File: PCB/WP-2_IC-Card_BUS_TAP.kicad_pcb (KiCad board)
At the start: 2 copper layers, 59.4 x 79.1 mm, 12 parts, among them J1 SMS-138-01-G-S, J2 Conn_02x19_Odd_Even, J3 TMS-138-01

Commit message: bus tap
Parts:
- moved key 1.84 mm to (102.1, 70.1)
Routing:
- net GND: vias 92 -> 93
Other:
- board text added: "GND /DET CE2 /CE1 /OE D0 D1 D2 D3 D4 D5 D6 D7 T2 S1 S2 A17 A16 A15 A14 A13 A12 A11 A10 A9 A8 A7 A6 A5 A4 A3 A2 A1 A0 R/W S3 BCHK VCC"
- board text added: "VCC"
- board text removed: "VBUS"

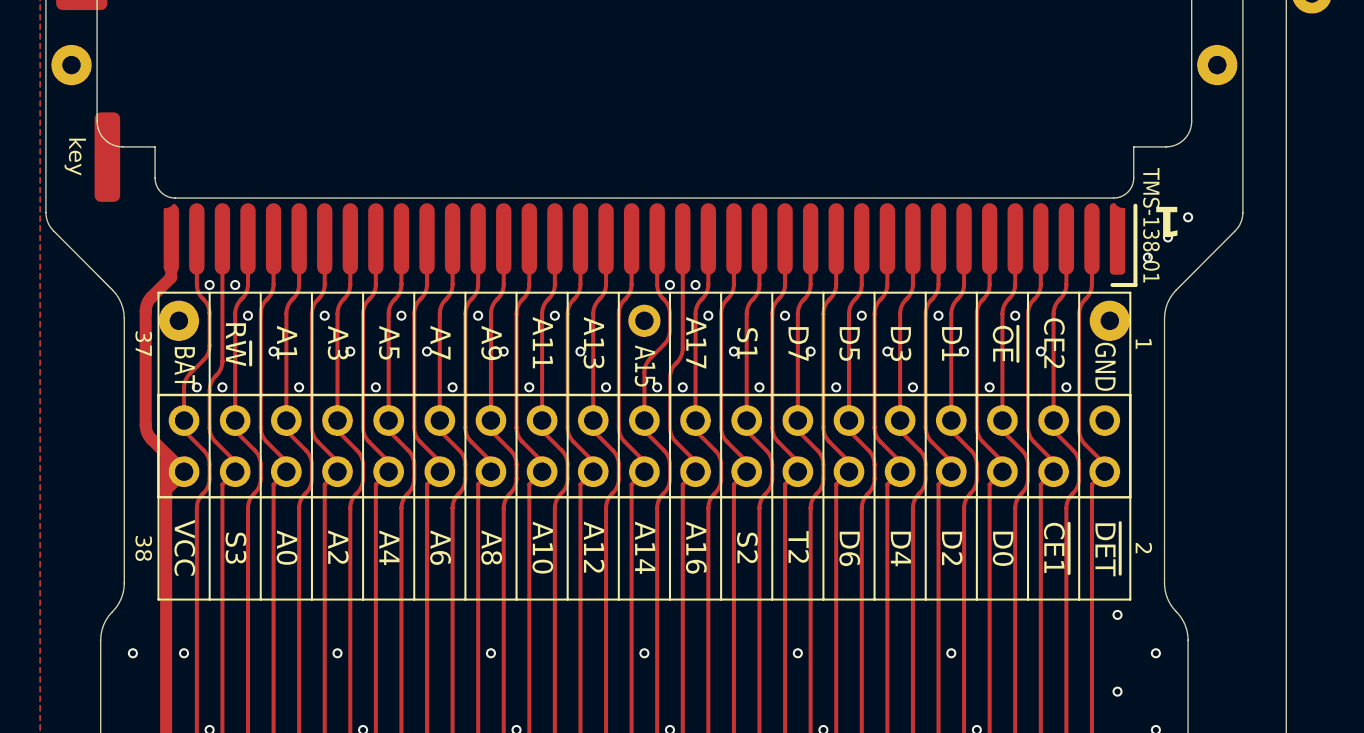
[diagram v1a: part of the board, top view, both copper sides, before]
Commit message: bus tap heal edge cuts
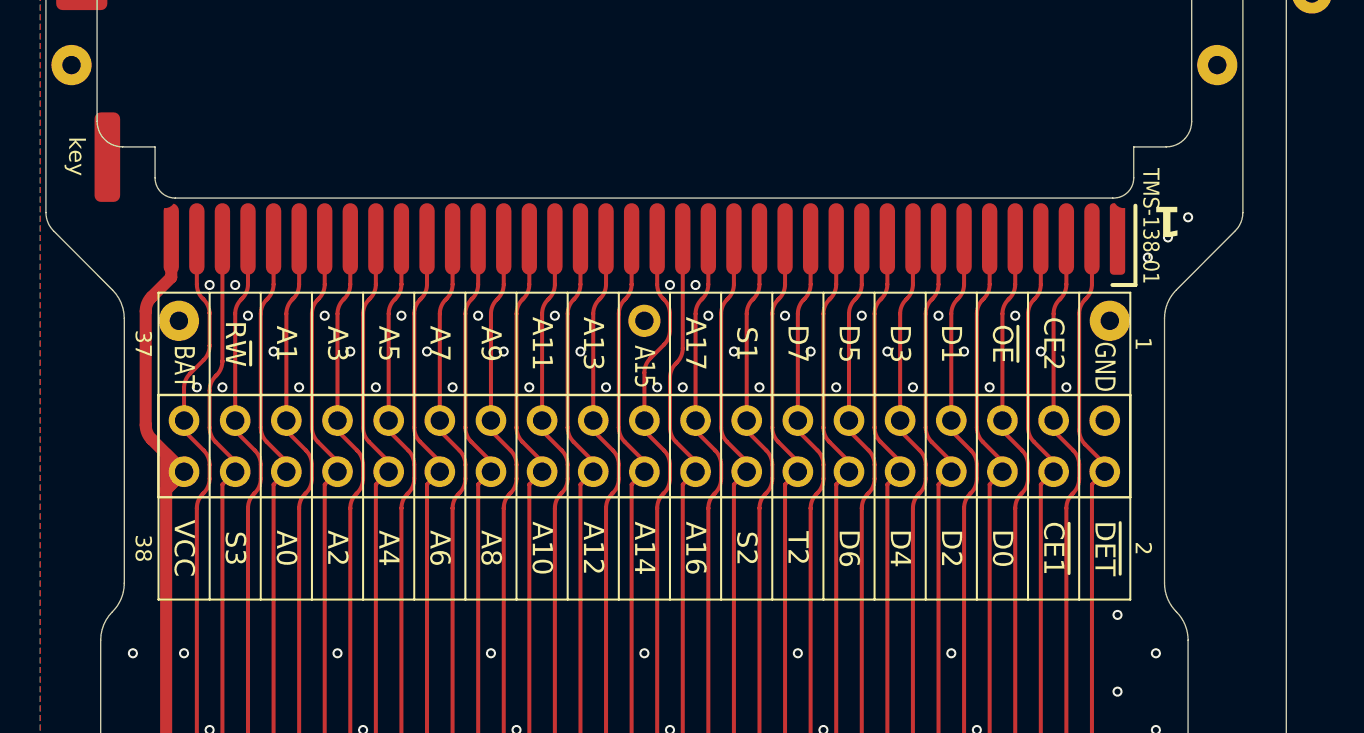
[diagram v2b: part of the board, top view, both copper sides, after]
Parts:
- N1: value WP-2_IC-Card_Cover_BUS_TAP -> WP-2_IC_Card_Cover_BUS_TAP

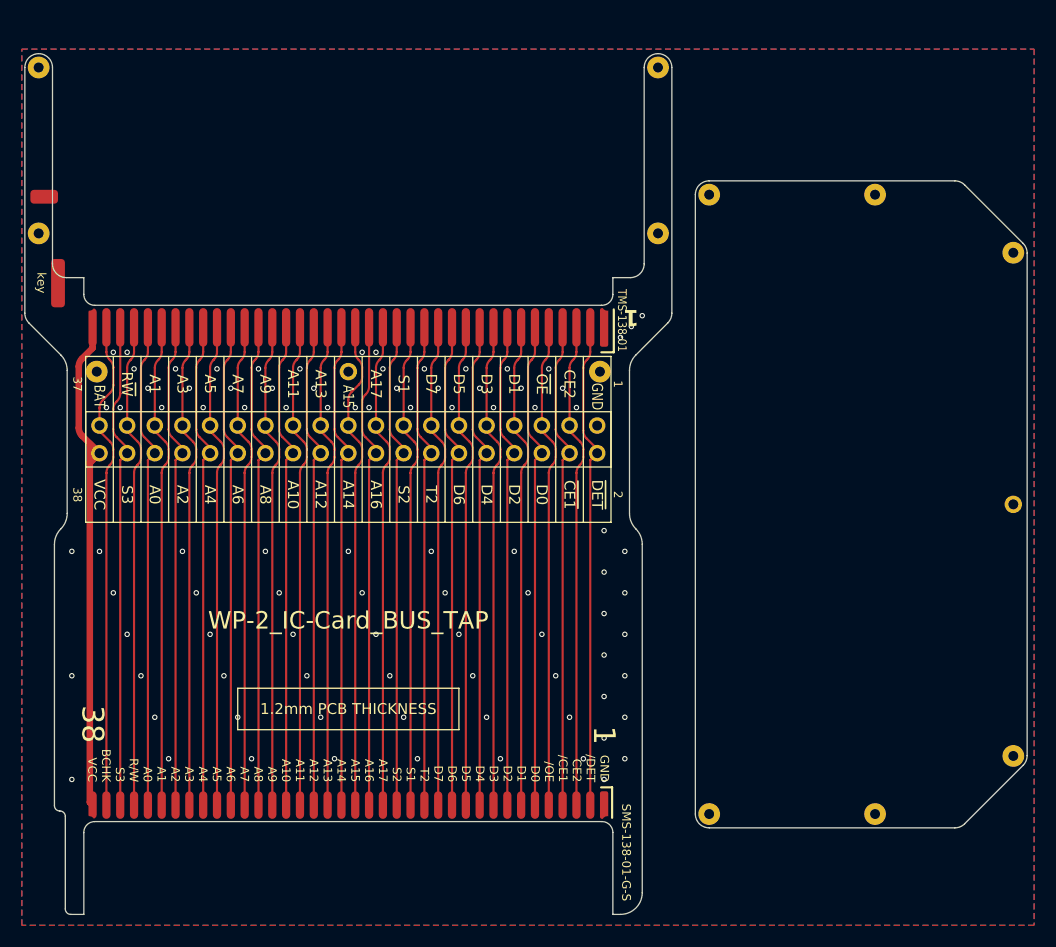
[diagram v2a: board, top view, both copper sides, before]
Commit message: bus tap: 40p idc, extra gnd, breakout vcc to measure current
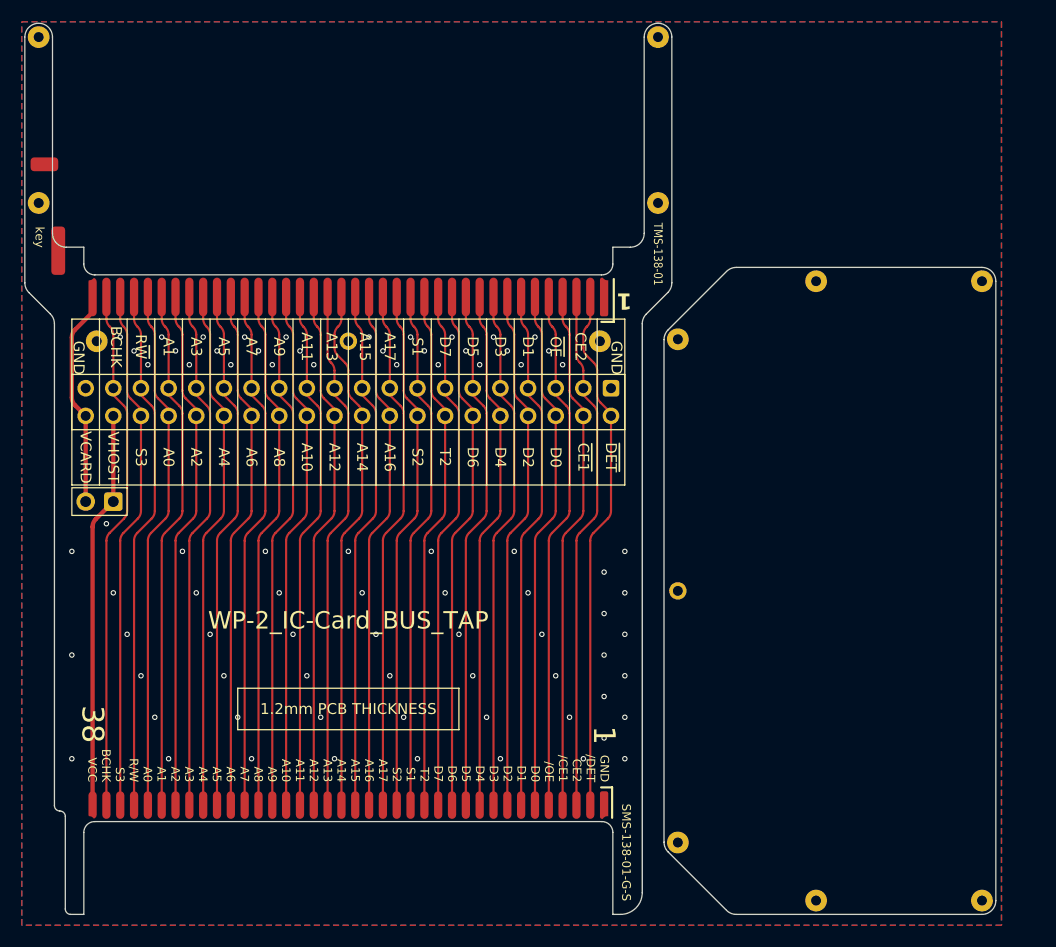
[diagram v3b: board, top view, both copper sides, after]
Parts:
- removed key: polarity_key, 000_LOCAL:polarity_key
- added JP1: VCC, 000_LOCAL:PinHeader_1x02_P2.54mm_Vertical, F.Cu at (108.4, 98.1)
- J2: footprint 000_LOCAL:PinHeader_2x19_P2.54mm -> 000_LOCAL:PinHeader_2x20_P2.54mm
- moved REF** 69.5 mm to (188.2, 134.7), turned to 180 degrees
- moved REF** 65.1 mm to (173.0, 134.7), turned to 180 degrees
- moved REF** 62.3 mm to (160.3, 129.4), turned to 180 degrees
- moved REF** 55.0 mm to (188.2, 77.8), turned to 180 degrees
- moved REF** 49.2 mm to (173.0, 77.8), turned to 180 degrees
- moved REF** 49.1 mm to (160.3, 83.2), turned to 180 degrees
- moved REF** 31.8 mm to (160.3, 106.3), turned to 180 degrees
- moved J2 3.66 mm to (154.1, 87.7)
- moved J3 2.79 mm to (130.0, 77.2)
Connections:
- J1 pad 38: VBUS -> VCC_HOST
- J2 pad 38: VBUS -> VCC_HOST
- J3 pad 38: VBUS -> VCC_CARD
- N1 pad : GND -> (no net)
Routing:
- net VBUS: track 45.6 -> 0.00 mm
- net VCC_HOST: track 0.00 -> 36.5 mm
- net VCC_CARD: track 0.00 -> 20.0 mm
- net /~{OE}: track 43.8 -> 48.0 mm
- net /CE2: track 43.8 -> 48.0 mm
- net /A17: track 43.8 -> 48.0 mm
- net /D5: track 43.8 -> 48.0 mm
- net /D7: track 43.8 -> 48.0 mm
- net /D1: track 43.8 -> 48.0 mm
- net /S1: track 43.8 -> 48.0 mm
- net /D3: track 43.8 -> 48.0 mm
- net /~{DET}: track 44.3 -> 48.4 mm
- net /A14: track 44.3 -> 48.4 mm
- net /D4: track 44.3 -> 48.0 mm
- net /D0: track 44.3 -> 48.0 mm
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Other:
- board size 59.4 x 79.1 mm -> 59.4 x 81.9 mm
- board text added: "BCHK"
- board text added: "VCARD"
- board text added: "VHOST"
- board text added: "key"
- board text removed: "2"
- board text removed: "37"
- board text removed: "BAT"
- board text removed: "Bottom Soldermask Full Coverage"
- board text removed: "VCC"

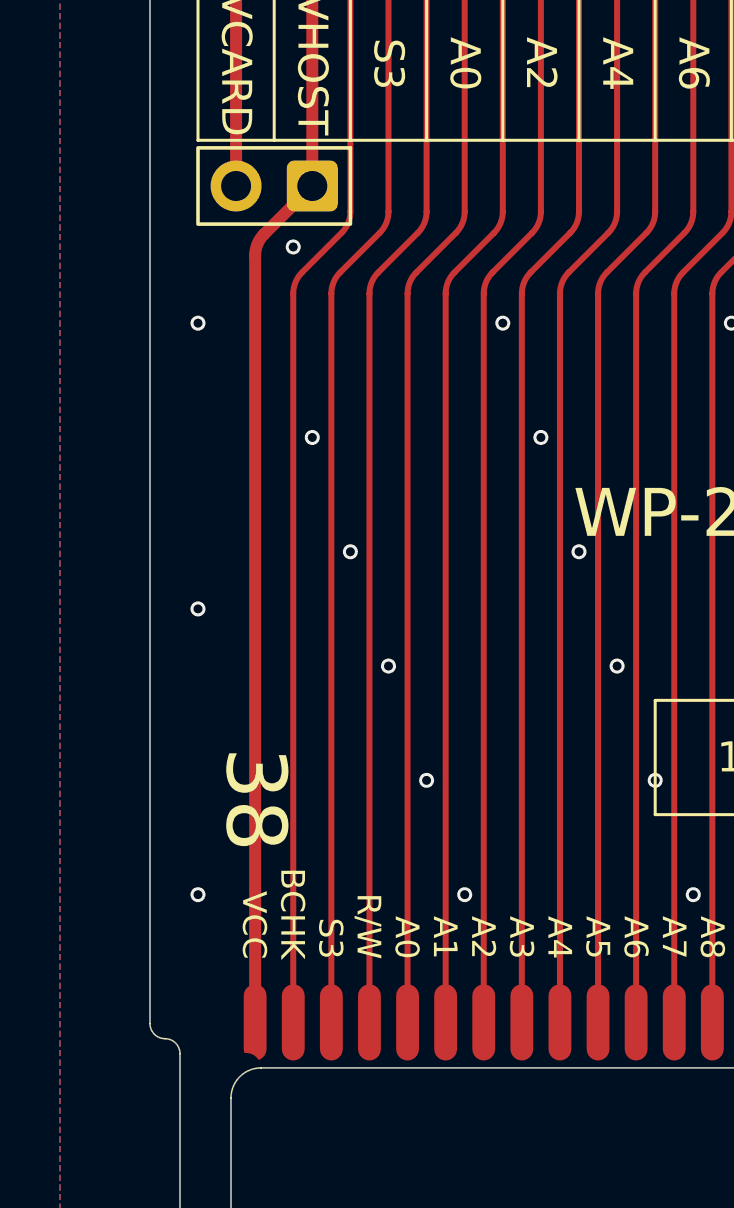
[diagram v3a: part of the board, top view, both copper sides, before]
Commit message: bus tap & breakout minor adjustments
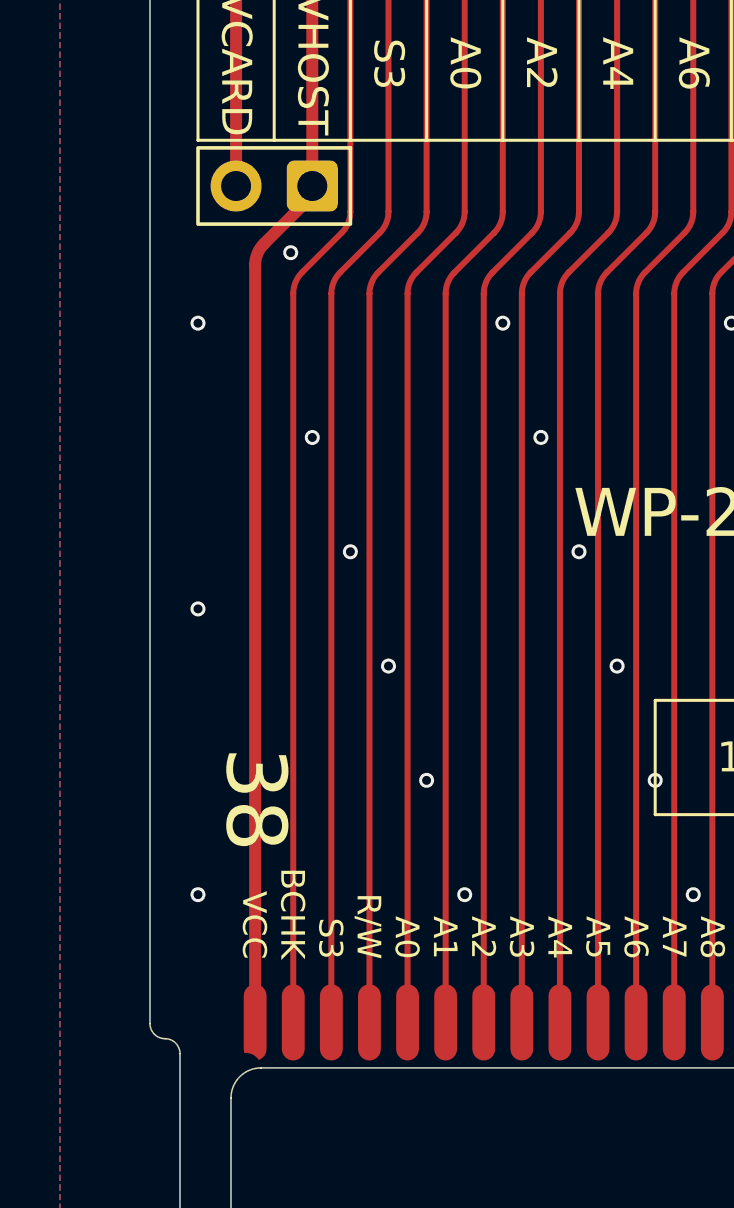
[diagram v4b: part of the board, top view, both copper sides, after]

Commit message: 3d
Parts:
- J2: value Conn_02x19_Odd_Even -> Conn_02x20_Odd_Even
